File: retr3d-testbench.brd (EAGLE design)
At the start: 76.6 x 52.4 mm, 72 parts, among them U1 ARDUINO-MEGAARDUINO_MEGA_MINI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

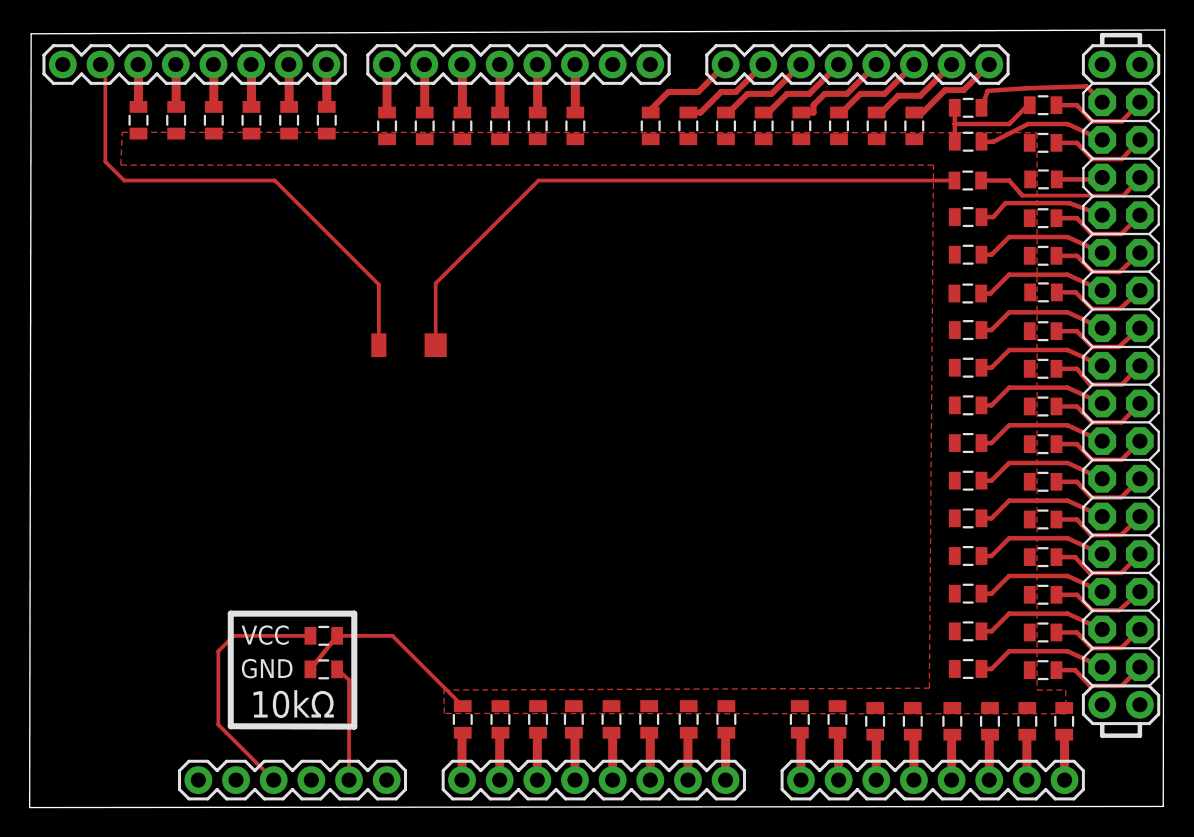
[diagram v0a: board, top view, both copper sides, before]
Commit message: Hatched fill for easier soldering
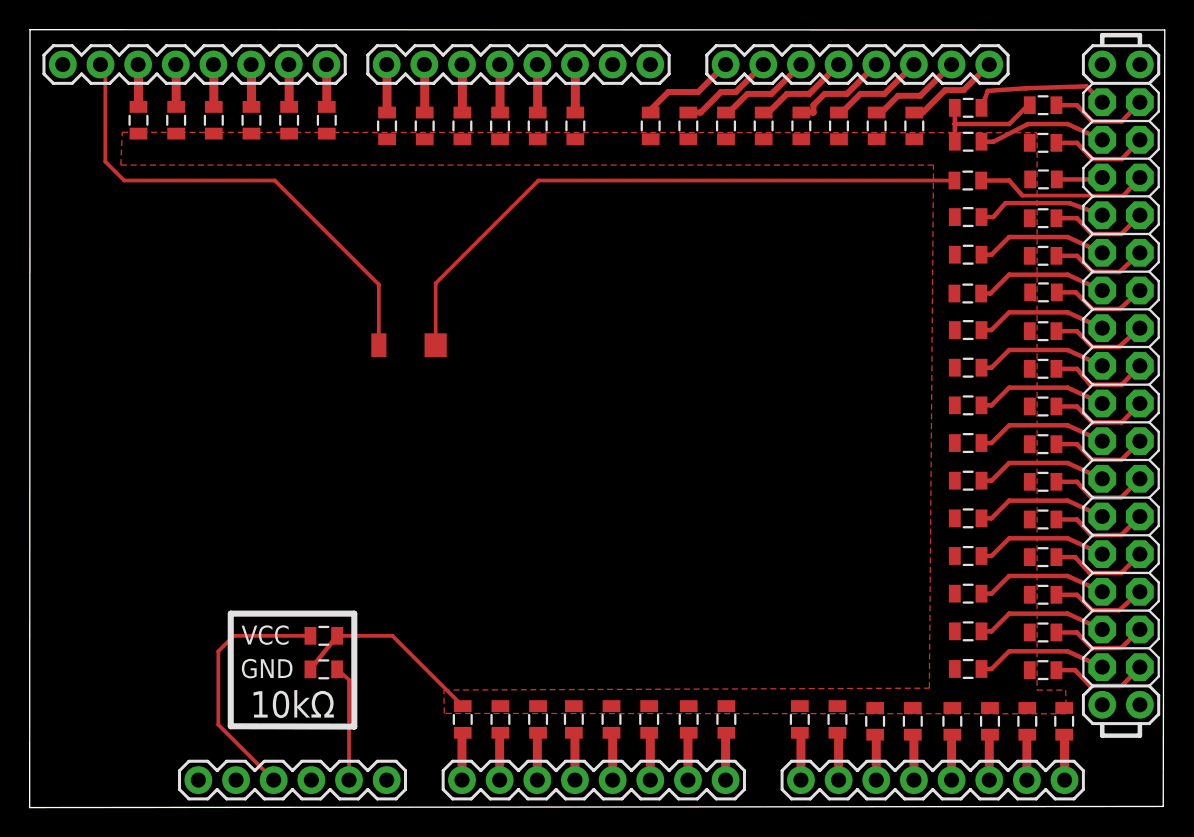
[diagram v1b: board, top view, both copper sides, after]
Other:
- board size 76.6 x 52.4 mm -> 76.6 x 52.5 mm
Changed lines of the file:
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@@
 <wire x1="22.8346" y1="18.669" x2="99.2888" y2="18.7452" width="0" layer="20"/>
 <wire x1="99.2888" y1="18.7452" x2="99.3904" y2="71.11" width="0" layer="20"/>
-<wire x1="99.3904" y1="71.11" x2="22.9362" y2="70.856" width="0" layer="20"/>
-<wire x1="22.9362" y1="70.856" x2="22.8346" y2="18.669" width="0" layer="20"/>
+<wire x1="99.3904" y1="71.11" x2="22.86" y2="71.1354" width="0" layer="20"/>
+<wire x1="22.86" y1="71.1354" x2="22.8346" y2="18.669" width="0" layer="20"/>
 <text x="37.6936" y="24.7396" size="1.778" layer="21">10kΩ</text>
 <wire x1="44.7294" y1="24.13" x2="44.7294" y2="31.75" width="0.4064" layer="21"/>
@@
 <contactref element="VCC" pad="1"/>
 <contactref element="GND" pad="1"/>
-<polygon width="0.4064" layer="1">
+<polygon width="0.4064" layer="1" spacing="2.54" pour="hatch">
 <vertex x="90.7796" y="64.1858"/>
 <vertex x="90.7796" y="26.5938"/>
